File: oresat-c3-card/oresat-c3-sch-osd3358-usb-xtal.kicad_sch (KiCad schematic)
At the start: 38 parts, among them U1 OSD3358-1G-ISM, U11 RCLAMP0504FB, Y1 ECS-240-12-30BQ-AEN-TR, Y2 ABS07-32.768KHZ-T

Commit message: Changed WDT tantalums to space-rated tantalums (fun) and fixed some BOM issues. Also possibly more silk screen cleanup.
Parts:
- C28, C29: DST Digi-Key -> DigiKey
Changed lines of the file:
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@@
 			)
 		)
-		(property "DST" "Digi-Key"
+		(property "DST" "DigiKey"
 			(at 160.02 119.38 0)
 			(effects
@@
 			)
 		)
-		(property "DST" "Digi-Key"
+		(property "DST" "DigiKey"
 			(at 160.02 104.14 0)
 			(effects

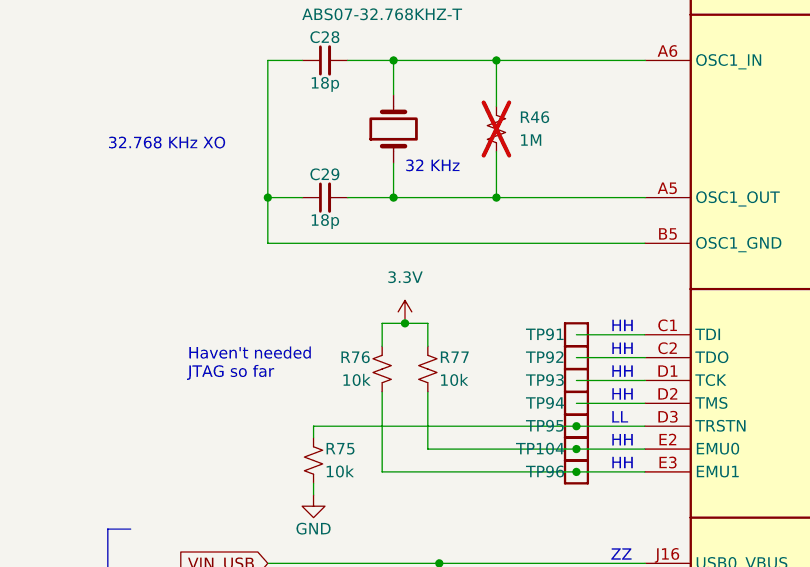
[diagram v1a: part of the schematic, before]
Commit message: Upgrade to KiCad 10, fix a few BOM entries, and we caught the first error! Go kicad 10.
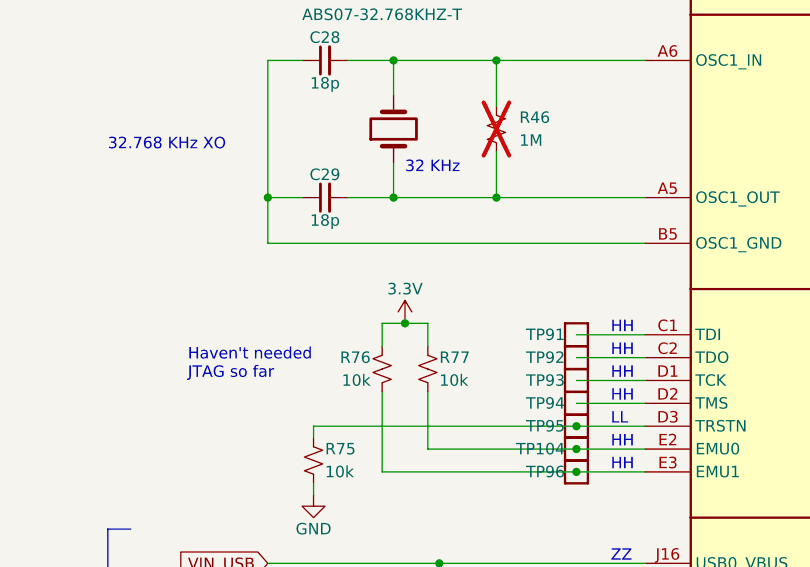
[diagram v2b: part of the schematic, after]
